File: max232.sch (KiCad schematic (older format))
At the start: 14 parts, among them J1 DB9, P1 CONN_6, P2 CONN_1, P3 CONN_1, P4 CONN_1, P5 CONN_1, Q1 MOSFET_N, Q2 MOSFET_N, U1 MAX232

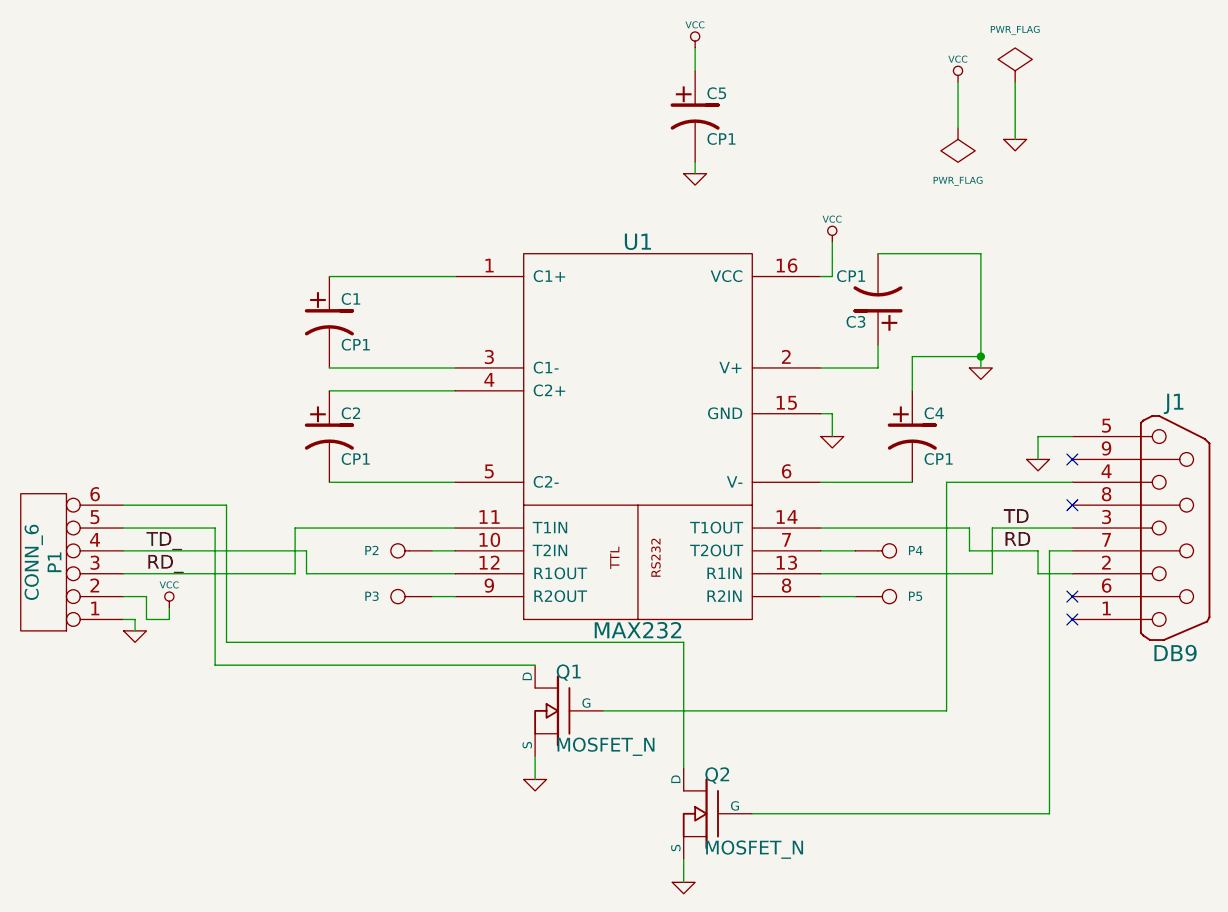
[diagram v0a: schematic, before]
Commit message: Added new version format of pcb (new KiCAD). Fixed name DTR<->RTS.
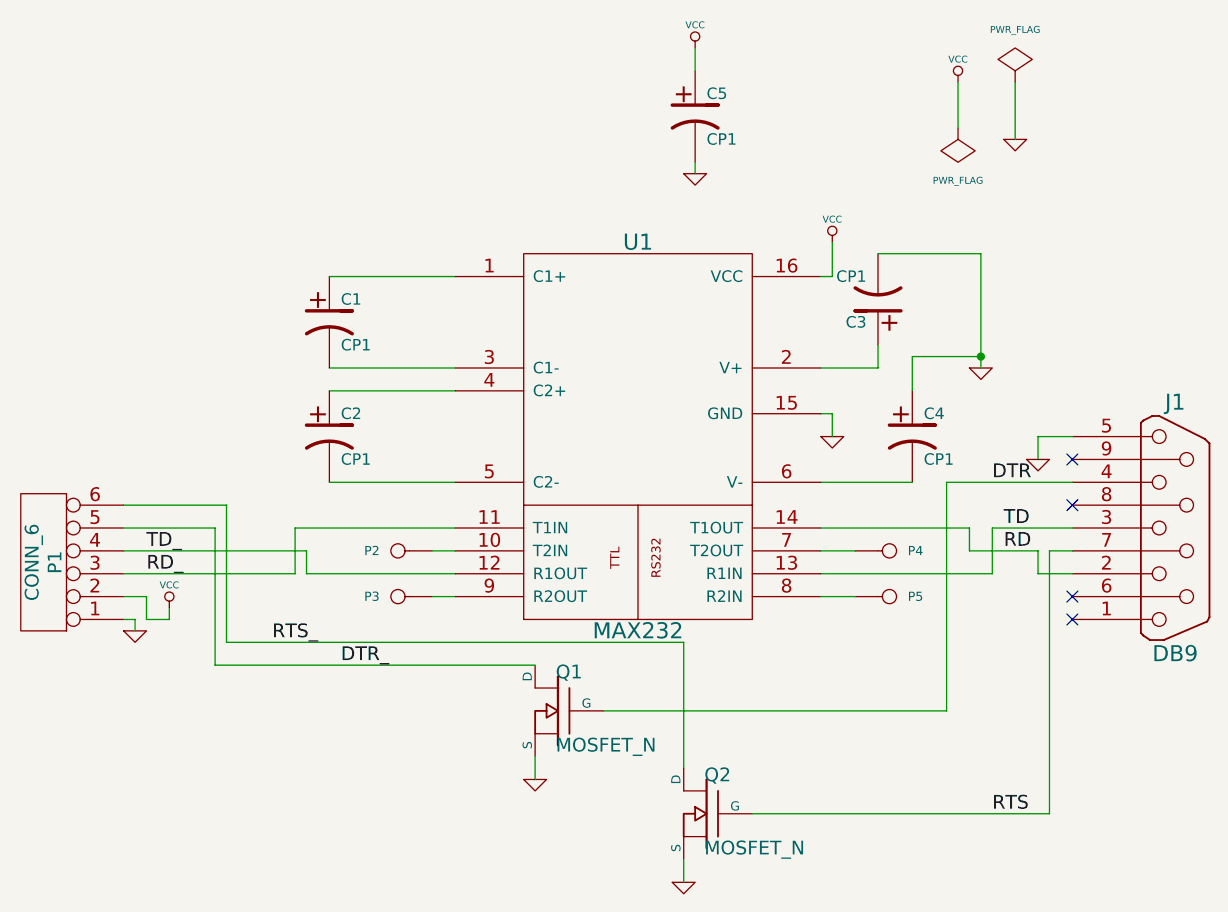
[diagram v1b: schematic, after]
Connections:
- net DTR: now reaches J1.4, Q1.G
- net RTS: now reaches J1.7 (P7), Q2.G
- net RTS_: now reaches P1.6, Q2.D
- net DTR_: now reaches P1.5, Q1.D
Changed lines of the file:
@@
 Sheet 1 1
 Title ""
-Date "8 sep 2013"
+Date "20 sep 2013"
 Rev ""
 Comp ""
@@
 	4950 2100 4950 2200
 $Comp
-L VCC #PWR?
+L VCC #PWR01
 U 1 1 522838C7
 P 5550 2950
-F 0 "#PWR?" H 5550 3050 30  0001 C CNN
+F 0 "#PWR01" H 5550 3050 30  0001 C CNN
 F 1 "VCC" H 5550 3050 30  0000 C CNN
 F 2 "" H 5550 2950 60  0001 C CNN
@@
 $EndComp
 $Comp
-L GND #PWR?
+L GND #PWR02
 U 1 1 52283890
 P 6200 3500
-F 0 "#PWR?" H 6200 3500 30  0001 C CNN
+F 0 "#PWR02" H 6200 3500 30  0001 C CNN
 F 1 "GND" H 6200 3430 30  0001 C CNN
 F 2 "" H 6200 3500 60  0001 C CNN
@@
 $EndComp
 $Comp
-L GND #PWR01
+L GND #PWR03
 U 1 1 520D15E7
 P 4900 5750
-F 0 "#PWR01" H 4900 5750 30  0001 C CNN
+F 0 "#PWR03" H 4900 5750 30  0001 C CNN
 F 1 "GND" H 4900 5680 30  0001 C CNN
 F 2 "" H 4900 5750 60  0001 C CNN
@@
 $EndComp
 $Comp
-L GND #PWR02
+L GND #PWR04
 U 1 1 520D15E5
 P 4250 5300
-F 0 "#PWR02" H 4250 5300 30  0001 C CNN
+F 0 "#PWR04" H 4250 5300 30  0001 C CNN
 F 1 "GND" H 4250 5230 30  0001 C CNN
 F 2 "" H 4250 5300 60  0001 C CNN
@@
 RD
 $Comp
-L PWR_FLAG #FLG03
+L PWR_FLAG #FLG05
 U 1 1 4FB299A7
 P 6100 2450
-F 0 "#FLG03" H 6100 2720 30  0001 C CNN
+F 0 "#FLG05" H 6100 2720 30  0001 C CNN
 F 1 "PWR_FLAG" H 6100 2680 30  0000 C CNN
 F 2 "" H 6100 2450 60  0001 C CNN
@@
 $EndComp
 $Comp
-L PWR_FLAG #FLG04
+L PWR_FLAG #FLG06
 U 1 1 4FB299A5
 P 6350 2250
-F 0 "#FLG04" H 6350 2520 30  0001 C CNN
+F 0 "#FLG06" H 6350 2520 30  0001 C CNN
 F 1 "PWR_FLAG" H 6350 2480 30  0000 C CNN
 F 2 "" H 6350 2250 60  0001 C CNN
@@
 $EndComp
 $Comp
-L GND #PWR05
+L GND #PWR07
 U 1 1 4FB29995
 P 6350 2500
-F 0 "#PWR05" H 6350 2500 30  0001 C CNN
+F 0 "#PWR07" H 6350 2500 30  0001 C CNN
 F 1 "GND" H 6350 2430 30  0001 C CNN
 F 2 "" H 6350 2500 60  0001 C CNN
@@
 $EndComp
 $Comp
-L VCC #PWR06
+L VCC #PWR08
 U 1 1 4FB29992
 P 6100 2250
-F 0 "#PWR06" H 6100 2350 30  0001 C CNN
+F 0 "#PWR08" H 6100 2350 30  0001 C CNN
 F 1 "VCC" H 6100 2350 30  0000 C CNN
 F 2 "" H 6100 2250 60  0001 C CNN
@@
 NoConn ~ 6600 4600
 $Comp
-L GND #PWR07
+L GND #PWR09
 U 1 1 4FB2981A
 P 6450 3900
-F 0 "#PWR07" H 6450 3900 30  0001 C CNN
+F 0 "#PWR09" H 6450 3900 30  0001 C CNN
 F 1 "GND" H 6450 3830 30  0001 C CNN
 F 2 "" H 6450 3900 60  0001 C CNN
@@
 $EndComp
 $Comp
-L GND #PWR08
+L GND #PWR010
 U 1 1 4FB29682
 P 2500 4650
-F 0 "#PWR08" H 2500 4650 30  0001 C CNN
+F 0 "#PWR010" H 2500 4650 30  0001 C CNN
 F 1 "GND" H 2500 4580 30  0001 C CNN
 F 2 "" H 2500 4650 60  0001 C CNN
@@
 $EndComp
 $Comp
-L VCC #PWR09
+L VCC #PWR011
 U 1 1 4FB2967B
 P 2650 4550
-F 0 "#PWR09" H 2650 4650 30  0001 C CNN
+F 0 "#PWR011" H 2650 4650 30  0001 C CNN
 F 1 "VCC" H 2650 4650 30  0000 C CNN
 F 2 "" H 2650 4550 60  0001 C CNN
@@
 $EndComp
 $Comp
-L GND #PWR011
+L GND #PWR012
 U 1 1 4FB2956D
 P 5550 3800
-F 0 "#PWR011" H 5550 3800 30  0001 C CNN
+F 0 "#PWR012" H 5550 3800 30  0001 C CNN
 F 1 "GND" H 5550 3730 30  0001 C CNN
 F 2 "" H 5550 3800 60  0001 C CNN
@@
 $EndComp
 $Comp
-L GND #PWR012
+L GND #PWR013
 U 1 1 4FB29531
 P 4950 2650
-F 0 "#PWR012" H 4950 2650 30  0001 C CNN
+F 0 "#PWR013" H 4950 2650 30  0001 C CNN
 F 1 "GND" H 4950 2580 30  0001 C CNN
 F 2 "" H 4950 2650 60  0001 C CNN
@@
 $EndComp
 $Comp
-L VCC #PWR013
+L VCC #PWR014
 U 1 1 4FB294D8
 P 4950 2100
-F 0 "#PWR013" H 4950 2200 30  0001 C CNN
+F 0 "#PWR014" H 4950 2200 30  0001 C CNN
 F 1 "VCC" H 4950 2200 30  0000 C CNN
 F 2 "" H 4950 2100 60  0001 C CNN
@@
 	1    0    0    -1
 $EndComp
+Text Label 6250 4000 0    60   ~ 0
+DTR
+Text Label 6250 5450 0    60   ~ 0
+RTS
+Text Label 3400 4800 0    60   ~ 0
+DTR_
+Text Label 3100 4700 0    60   ~ 0
+RTS_
 $EndSCHEMATC
